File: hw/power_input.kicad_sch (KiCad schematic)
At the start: 23 parts, among them Q101 P-ch, |Vds|>=80V, Q102 100V 10mOhm N-ch, U101 TLV3201, U102 UCC27517A

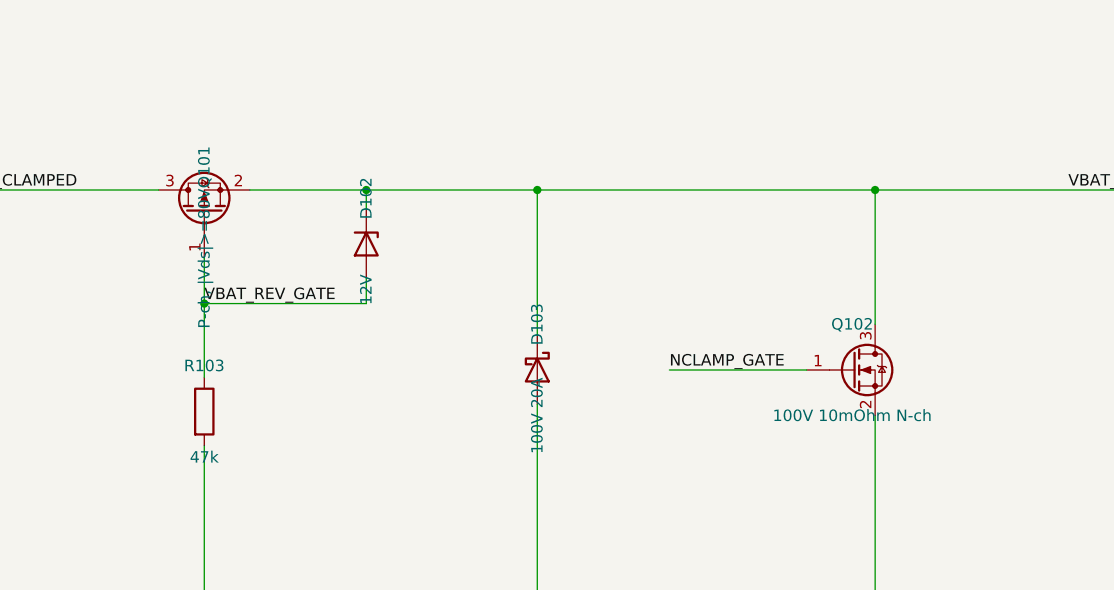
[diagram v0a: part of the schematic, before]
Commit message: Choose the power FETs, and draw DPAK parts with G-D-S symbols
Four part numbers for all sixteen power FETs, each against a retrieved
datasheet:
  SQD50P08-25L    reverse-battery P-FET, 31 mOhm max at -4.5 V
  IPD90N10S4-06   x8: negative clamp, metering, EGR bridge, injector
                  battery switches; 6.7 mOhm at 10 V, +/-20 V Vgs
                  (the logic-level -S4L-06 is +/-16 V, and every one of
                  these gates is driven from 12V_GATE)
  SQM85N15-19     x5: injector boost-side and low-side, 19 mOhm, TO-263
  DMN15H310SK3    boost switch, Rds(on) specified at a 4 V gate

Every FET was drawn as Q_NMOS_GSD, the SOT-23 order. DPAK and D2PAK are
G-D-S with the drain on the tab, so a TO-252 footprint on that symbol
puts the source on the tab. The power FETs now use Q_NMOS_GDS /
Q_PMOS_GDS: same pin positions, verified against the library, drains
on pin 2 in the netlist.

Checks that had run on placeholders now use the chosen parts: bootstrap
droop at 120 nC max (126 mV, was 60 nC), cranking duty including the
boost switch and sense drop (94.8% of 97.0%), and the pulldowns' 500 pF
Crss sizing against the worst chosen part (300 pF).

24/24 sim blocks, netlist gate passing, 58 of 297 parts with footprints.
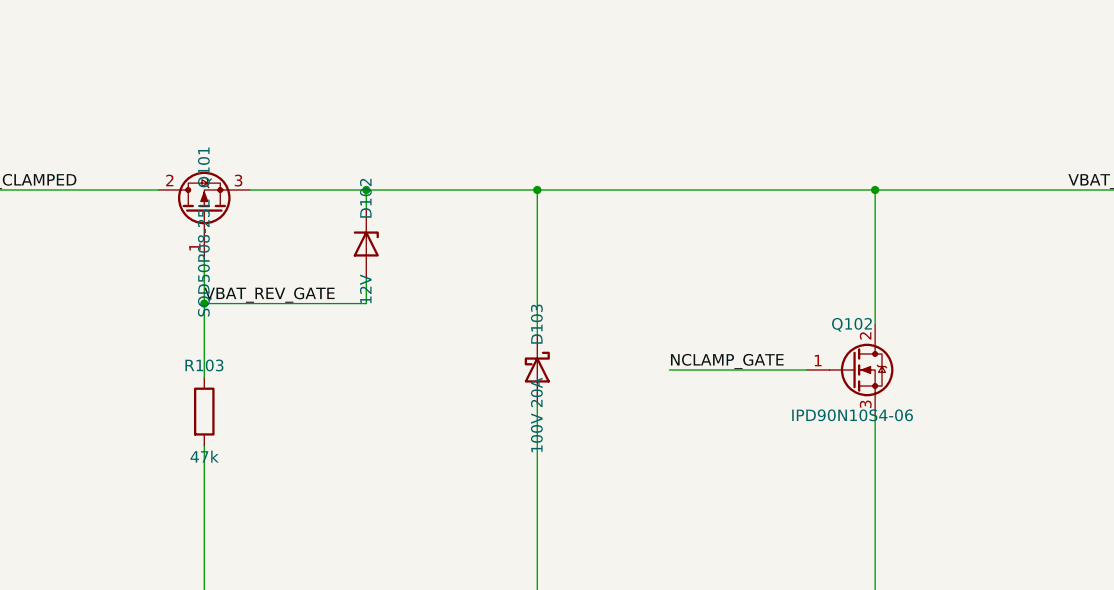
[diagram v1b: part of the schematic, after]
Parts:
- removed Q101: P-ch, |Vds|>=80V, symbol Device:Q_PMOS_GSD
- removed Q102: 100V 10mOhm N-ch, symbol Device:Q_NMOS_GSD
- added Q101: SQD50P08-25L, Package_TO_SOT_SMD:TO-252-2, symbol Device:Q_PMOS_GDS
- added Q102: IPD90N10S4-06, Package_TO_SOT_SMD:TO-252-2, symbol Device:Q_NMOS_GDS
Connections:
- net GND: now also Q102.3 (S)
- net NCLAMP_GATE: now also Q102.1 (G)
- net VBAT_CLAMPED: now also Q101.2 (D)
- net VBAT_PROT: now also Q101.3 (S), Q102.2 (D)
- net VBAT_REV_GATE: now also Q101.1 (G)
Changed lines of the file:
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@@
     (effects (font (size 1.27 1.27)) (justify left bottom))
   )
-  (symbol (lib_id "Device:Q_PMOS_GSD") (at 268.0 82.54 90) (unit 1)
+  (symbol (lib_id "Device:Q_PMOS_GDS") (at 268.0 82.54 90) (unit 1)
     (in_bom yes) (on_board yes) (fields_autoplaced)
     (property "Reference" "Q101" (id 0) (at 268 77.46000000000001 0)
       (effects (font (size 1.27 1.27)))
     )
-    (property "Value" "P-ch, |Vds|>=80V" (id 1) (at 268 87.62 0)
+    (property "Value" "SQD50P08-25L" (id 1) (at 268 87.62 0)
       (effects (font (size 1.27 1.27)))
     )
-    (property "Footprint" "" (id 2) (at 268 82.54 0)
+    (property "Footprint" "Package_TO_SOT_SMD:TO-252-2" (id 2) (at 268 82.54 0)
       (effects (font (size 1.27 1.27)) hide)
     )
@@
       (effects (font (size 1.27 1.27)) hide)
     )
-    (property "Source" "reverse_battery.cir path B -- modelled as a P-FET all along" (id 4) (at 268 82.54 0)
+    (property "MPN" "SQD50P08-25L" (id 4) (at 268 82.54 0)
       (effects (font (size 1.27 1.27)) hide)
     )
-    (property "Note" "Drain to battery, source to load. |Vds| worst case is 47.8 V, blocking pulse 1 with the load side clamped near zero; 80 V class anyway, by the board's own rail rule." (id 5) (at 268 82.54 0)
+    (property "Source" "reverse_battery.cir path B -- modelled as a P-FET all along" (id 5) (at 268 82.54 0)
       (effects (font (size 1.27 1.27)) hide)
     )
-    (property "Rds_on" "<=40 mOhm at Vgs = -4.5 V: 0.2 V at 5 A against reverse_battery.cir's 0.3 V requirement, and specified at -4.5 V because at a 6 V cranking dip that is all the gate gets" (id 6) (at 268 82.54 0)
+    (property "Note" "Drain to battery, source to load. |Vds| worst case is 47.8 V, blocking pulse 1 with the load side clamped near zero; 80 V class anyway, by the board's own rail rule." (id 6) (at 268 82.54 0)
+      (effects (font (size 1.27 1.27)) hide)
+    )
+    (property "Rds_on" "31 mOhm max at -4.5 V (Vishay SQD50P08-25L; req. <=40): 0.16 V at 5 A against reverse_battery.cir's 0.3 V requirement, and specified at -4.5 V because at a 6 V cranking dip that is all the gate gets" (id 7) (at 268 82.54 0)
       (effects (font (size 1.27 1.27)) hide)
     )
@@
   (junction (at 305.0 80.0) (diameter 0) (color 0 0 0 0)
   )
-  (symbol (lib_id "Device:Q_NMOS_GSD") (at 340.0 100.0 0) (unit 1)
+  (symbol (lib_id "Device:Q_NMOS_GDS") (at 340.0 100.0 0) (unit 1)
     (in_bom yes) (on_board yes) (fields_autoplaced)
     (property "Reference" "Q102" (id 0) (at 340 94.92 0)
       (effects (font (size 1.27 1.27)))
     )
-    (property "Value" "100V 10mOhm N-ch" (id 1) (at 340 105.08 0)
+    (property "Value" "IPD90N10S4-06" (id 1) (at 340 105.08 0)
       (effects (font (size 1.27 1.27)))
     )
-    (property "Footprint" "" (id 2) (at 340 100.0 0)
+    (property "Footprint" "Package_TO_SOT_SMD:TO-252-2" (id 2) (at 340 100.0 0)
       (effects (font (size 1.27 1.27)) hide)
     )
@@
       (effects (font (size 1.27 1.27)) hide)
     )
-    (property "Source" "bom_requirements NEG-CLAMP; negative_pulses.cir Scl1" (id 4) (at 340 100.0 0)
+    (property "MPN" "IPD90N10S4-06" (id 4) (at 340 100.0 0)
       (effects (font (size 1.27 1.27)) hide)
     )
-    (property "Note" "Active clamp. 15 A through 5 mOhm is 75 mV, against a -0.3 V rating no junction device can meet (0.367 V junction + 0.180 V bulk)." (id 5) (at 340 100.0 0)
+    (property "Source" "bom_requirements NEG-CLAMP; negative_pulses.cir Scl1" (id 5) (at 340 100.0 0)
       (effects (font (size 1.27 1.27)) hide)
     )
-    (property "Vds" "100 V class. It was 40 V until 22 Sep 2026 -- sized for the negative pulses it clamps, with its drain on a node pulse 2a drives to +73.3 V. 40 V had zero margin on the load dump alone." (id 6) (at 340 100.0 0)
+    (property "Note" "Active clamp. 15 A through 5 mOhm is 75 mV, against a -0.3 V rating no junction device can meet (0.367 V junction + 0.180 V bulk)." (id 6) (at 340 100.0 0)
       (effects (font (size 1.27 1.27)) hide)
     )
-    (property "Rds_on" "10 mOhm max at Vgs=4.5 V" (id 7) (at 340 100.0 0)
+    (property "Vds" "100 V class. It was 40 V until 22 Sep 2026 -- sized for the negative pulses it clamps, with its drain on a node pulse 2a drives to +73.3 V. 40 V had zero margin on the load dump alone." (id 7) (at 340 100.0 0)
       (effects (font (size 1.27 1.27)) hide)
     )
+    (property "Rds_on" "6.7 mOhm max at Vgs = 10 V (Infineon IPD90N10S4-06). Gate from UCC27517A on 12V_GATE, so the 10 V point is the one that applies; +/-20 V Vgs" (id 8) (at 340 100.0 0)
+      (effects (font (size 1.27 1.27)) hide)
+    )
